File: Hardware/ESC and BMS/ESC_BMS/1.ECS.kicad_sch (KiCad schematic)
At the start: 49 parts, among them Q201 SiR696DP, Q202 SiR696DP, Q203 SiR696DP, Q204 SiR696DP, Q205 SiR696DP, Q206 SiR696DP, U201 74AUC2G08, U202 74AUC2G08, U203 IR2301, U204 IR2301, U205 SN74LVC1G00DBV, U206 SN74LVC1G00DBV, U207 74AUC2G08, U208 TL331, U209 IR2301, U210 SN74LVC1G00DBV

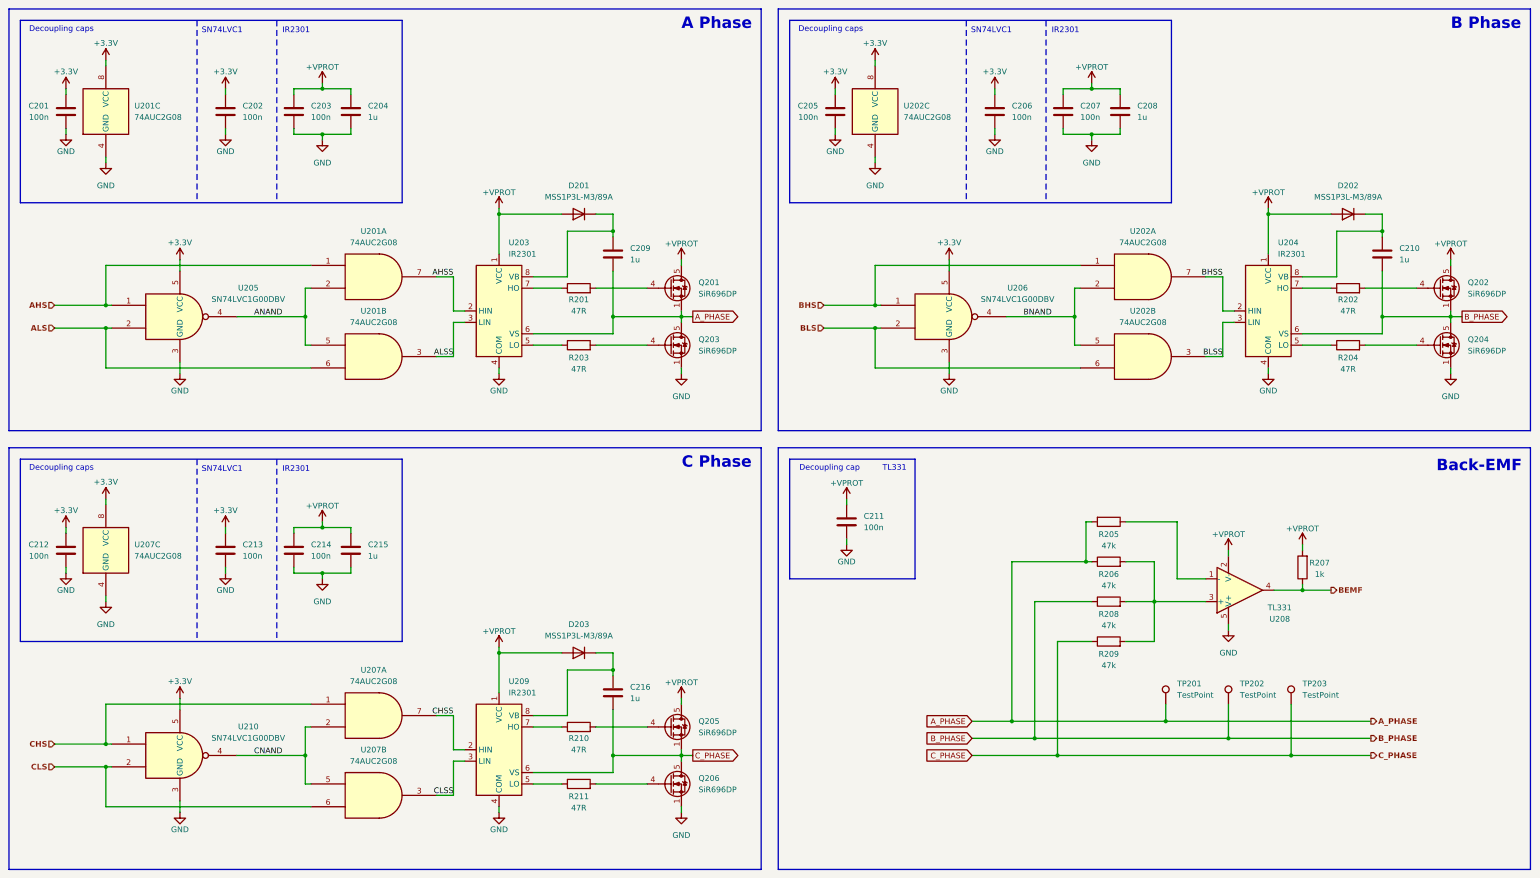
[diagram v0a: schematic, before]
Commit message: Updated 1.ECS.kicad_sch to put more caps and fix some nets
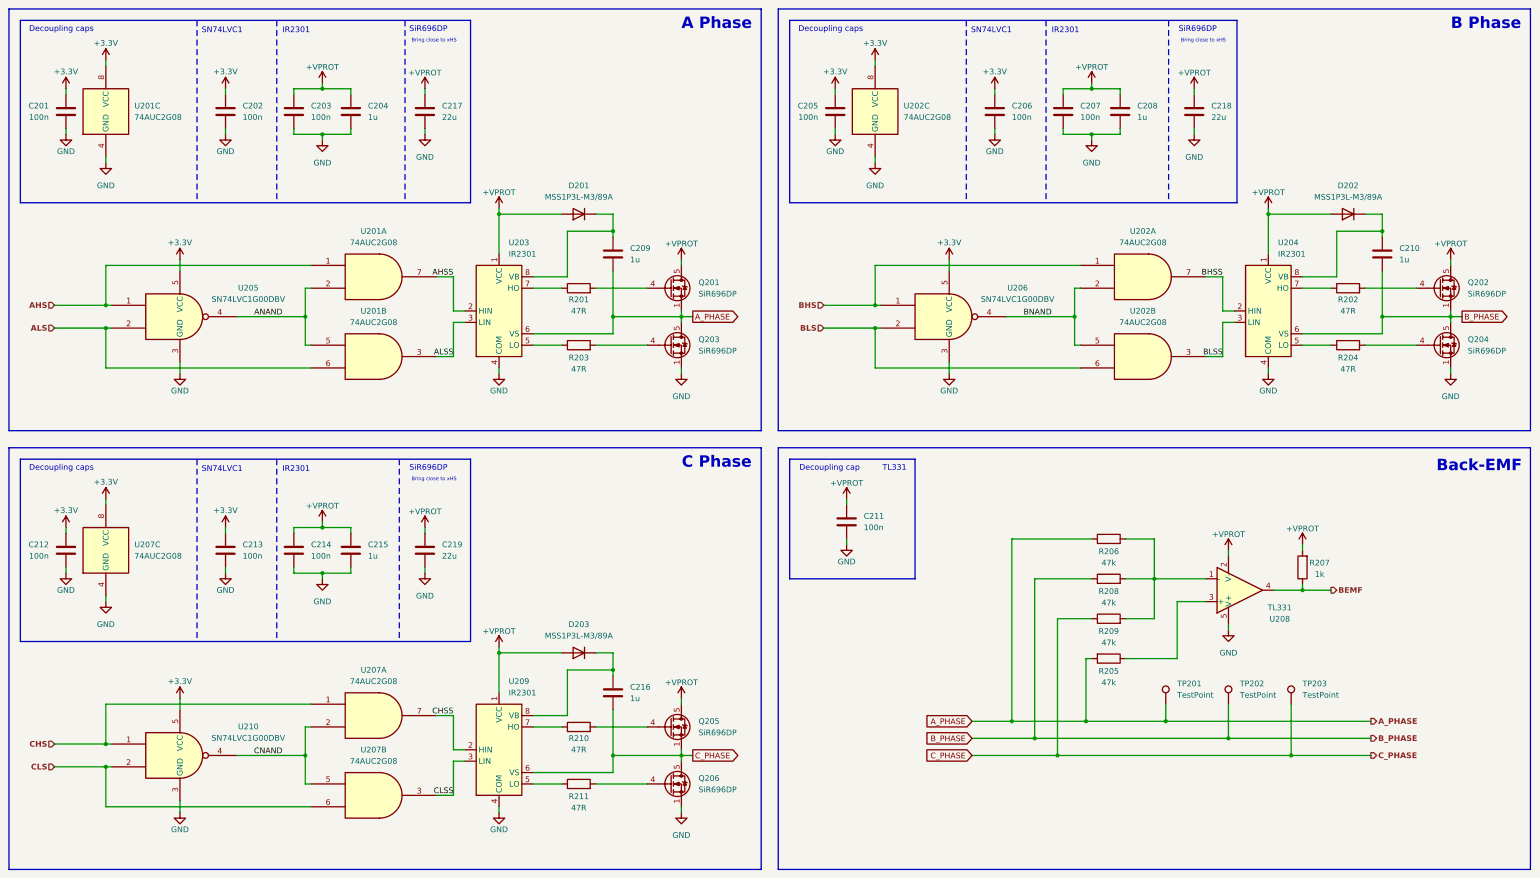
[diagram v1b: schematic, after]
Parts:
- added C217, C218, C219: 22u, Capacitor_SMD:C_0805_2012Metric_Pad1.18x1.45mm_HandSolder, symbol Device:C
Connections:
- net +VPROT: now also C217.1, C218.1, C219.1
- net GND: now also C217.2, C218.2, C219.2
- net at R206.2, R208.2, R209.2: now also U208.1 (-); no longer U208.3 (+)
- net at R205.1: now also U208.3 (+); no longer U208.1 (-)
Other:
- note added: "Bring close to xHS"
- note added: "SiR696DP"
- moved on the sheet: R205, R206, R208, R209

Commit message: initial BMS work
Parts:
- renumbered C217 to C10, C219 to C11, C209 to C12, C216 to C13, C205 to C14, C211 to C15, C206 to C16, C207 to C17, C208 to C18, C218 to C19, C201 to C2, C210 to C20, C212 to C3, C202 to C4, C213 to C5, C203 to C6, C214 to C7, C204 to C8, C215 to C9, D201 to D2, D203 to D3, D202 to D4, Q201 to Q2, Q203 to Q3, Q205 to Q4, Q206 to Q5, Q202 to Q6, Q204 to Q7, R207 to R10, R202 to R11, R204 to R12, R201 to R2, R203 to R3, R210 to R4, R211 to R5, R206 to R6, R208 to R7, R209 to R8, R205 to R9, TP201 to TP2, TP202 to TP3, TP203 to TP4, U208 to U10, U204 to U11, U201 to U2, U207 to U3, U205 to U4, U210 to U5, U203 to U6, U209 to U7, U202 to U8, U206 to U9
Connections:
- net +3.3V: now also R10.2
- net +VPROT: no longer R10.2

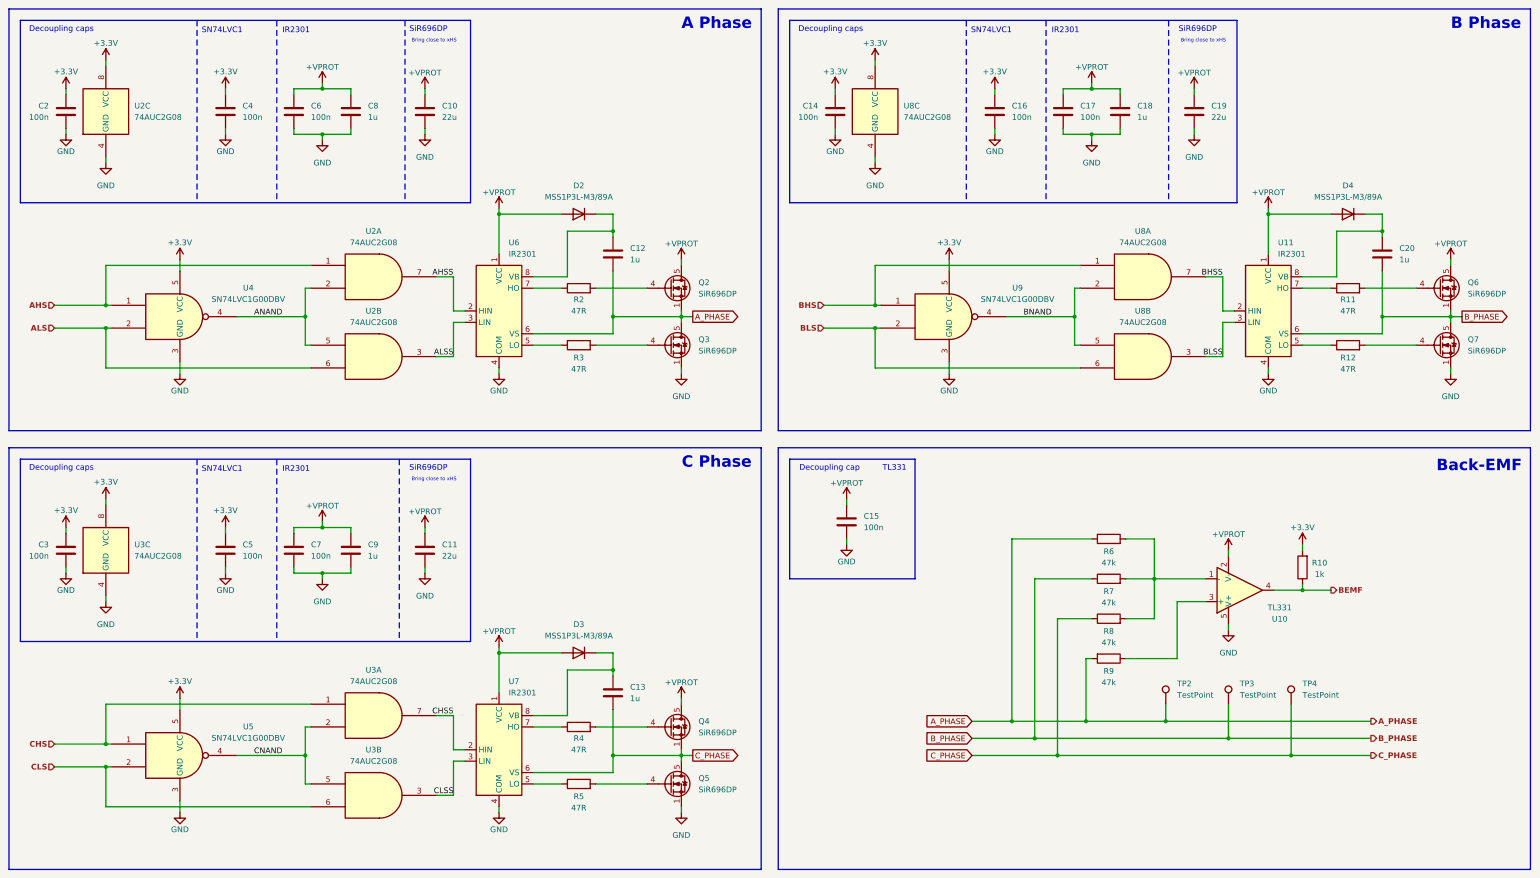
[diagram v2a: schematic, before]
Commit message: Simulations for BMS start and footprints
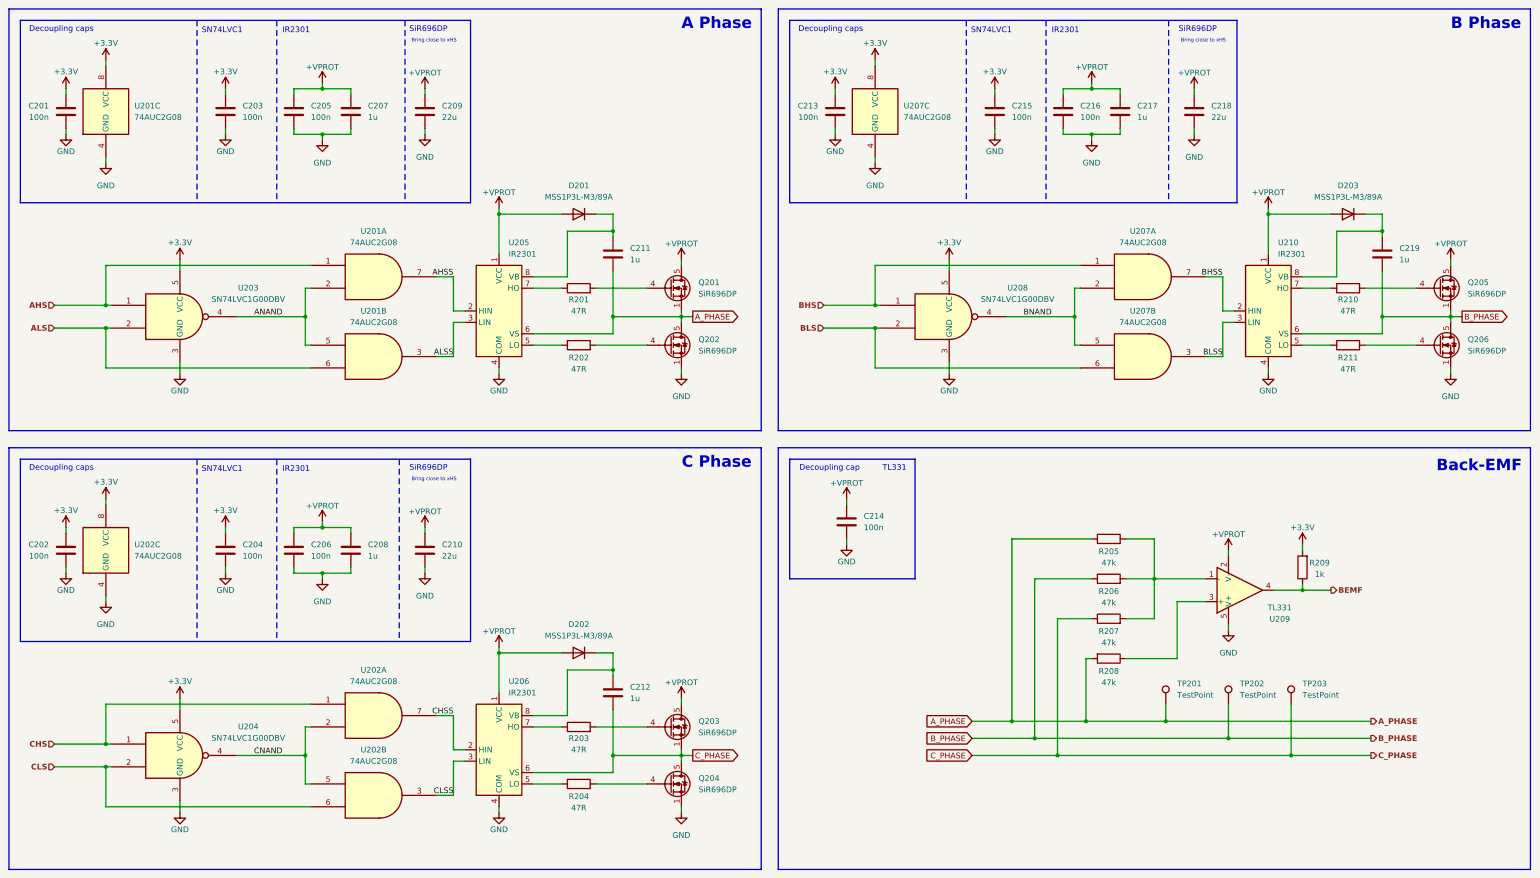
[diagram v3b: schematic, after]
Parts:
- renumbered C2 to C201, C3 to C202, C4 to C203, C5 to C204, C6 to C205, C7 to C206, C8 to C207, C9 to C208, C10 to C209, C11 to C210, C12 to C211, C13 to C212, C14 to C213, C15 to C214, C16 to C215, C17 to C216, C18 to C217, C19 to C218, C20 to C219, D2 to D201, D3 to D202, D4 to D203, Q2 to Q201, Q3 to Q202, Q4 to Q203, Q5 to Q204, Q6 to Q205, Q7 to Q206, R2 to R201, R3 to R202, R4 to R203, R5 to R204, R6 to R205, R7 to R206, R8 to R207, R9 to R208, R10 to R209, R11 to R210, R12 to R211, TP2 to TP201, TP3 to TP202, TP4 to TP203, U2 to U201, U3 to U202, U4 to U203, U5 to U204, U6 to U205, U7 to U206, U8 to U207, U9 to U208, U10 to U209, U11 to U210

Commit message: More BMS
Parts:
- TP201, TP202, TP203: footprint (none) -> TestPoint:TestPoint_Pad_D2.0mm
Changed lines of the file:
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@@
 			)
 		)
-		(property "Footprint" ""
+		(property "Footprint" "TestPoint:TestPoint_Pad_D2.0mm"
 			(at 317.5 196.85 0)
 			(effects
@@
 			)
 		)
-		(property "Footprint" ""
+		(property "Footprint" "TestPoint:TestPoint_Pad_D2.0mm"
 			(at 303.53 196.85 0)
 			(effects
@@
 			)
 		)
-		(property "Footprint" ""
+		(property "Footprint" "TestPoint:TestPoint_Pad_D2.0mm"
 			(at 331.47 196.85 0)
 			(effects

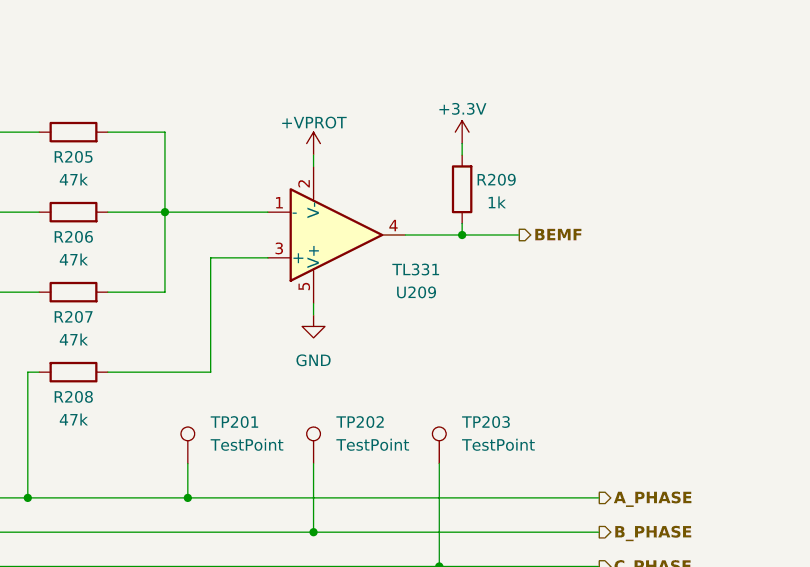
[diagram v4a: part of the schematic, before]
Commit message: ESC/BMS PCB started
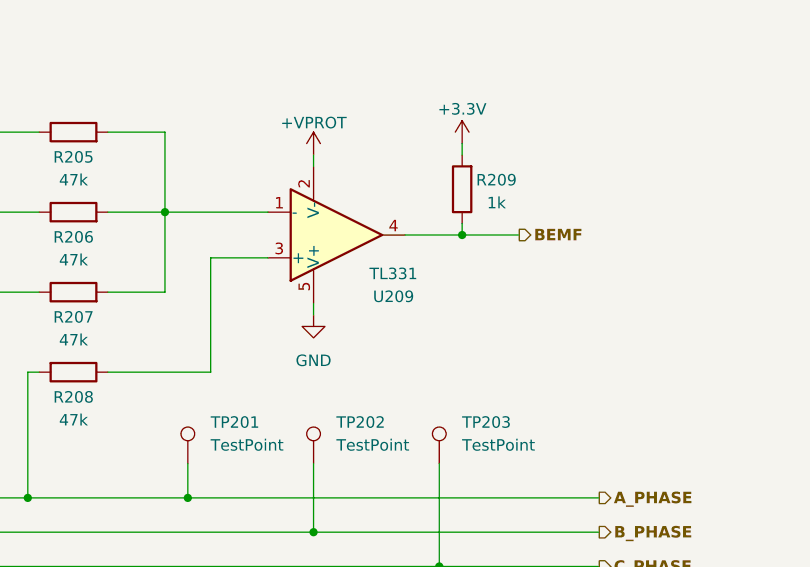
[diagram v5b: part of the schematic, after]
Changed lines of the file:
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@@
 		(dnp no)
 		(property "Reference" "U209"
-			(at 323.85 177.8702 0)
+			(at 321.31 178.308 0)
 			(effects
 				(font
@@
 		)
 		(property "Value" "TL331"
-			(at 323.85 175.3302 0)
+			(at 321.31 175.768 0)
 			(effects
 				(font

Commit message: ESC/BMS board done fully fully
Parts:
- TP201, TP202, TP203: footprint TestPoint:TestPoint_Pad_D2.0mm -> TestPoint:TestPoint_Pad_D1.0mm
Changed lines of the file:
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@@
 			)
 		)
-		(property "Footprint" "TestPoint:TestPoint_Pad_D2.0mm"
+		(property "Footprint" "TestPoint:TestPoint_Pad_D1.0mm"
 			(at 317.5 196.85 0)
 			(effects
@@
 			)
 		)
-		(property "Footprint" "TestPoint:TestPoint_Pad_D2.0mm"
+		(property "Footprint" "TestPoint:TestPoint_Pad_D1.0mm"
 			(at 303.53 196.85 0)
 			(effects
@@
 			)
 		)
-		(property "Footprint" "TestPoint:TestPoint_Pad_D2.0mm"
+		(property "Footprint" "TestPoint:TestPoint_Pad_D1.0mm"
 			(at 331.47 196.85 0)
 			(effects

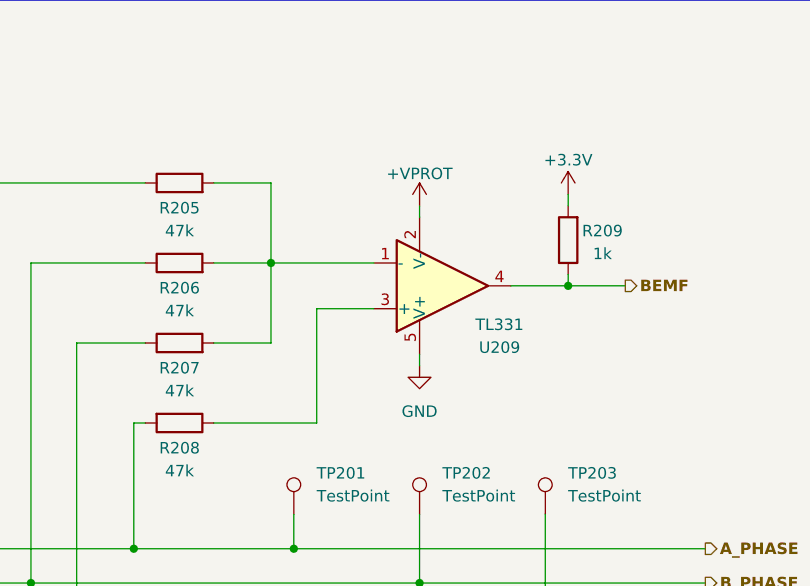
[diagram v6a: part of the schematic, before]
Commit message: fixed vprot and gnd comp error
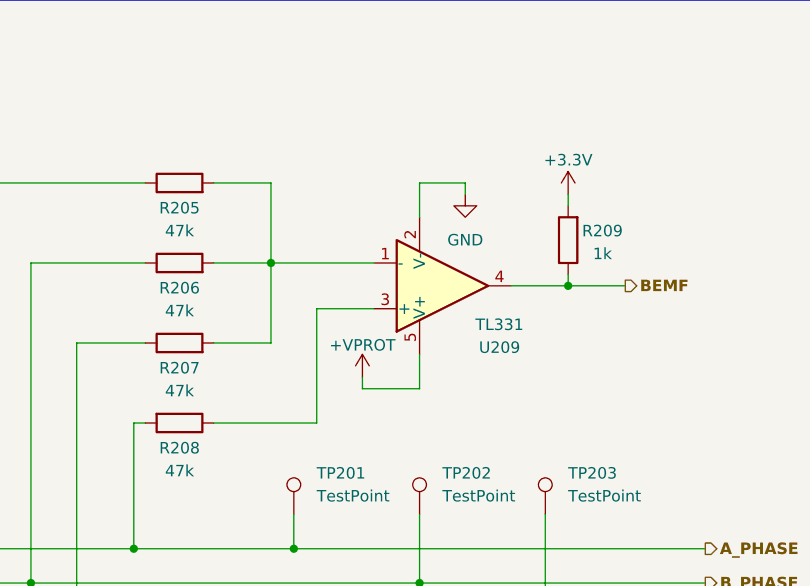
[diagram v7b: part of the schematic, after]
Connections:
- net +VPROT: now also U209.5 (V+); no longer U209.2 (V-)
- net GND: now also U209.2 (V-); no longer U209.5 (V+)
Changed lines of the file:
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@@
 	(wire
 		(pts
+			(xy 312.42 160.02) (xy 312.42 163.83)
+		)
+		(stroke
+			(width 0)
+			(type default)
+		)
+	)
+	(wire
+		(pts
 			(xy 133.35 157.48) (xy 133.35 158.75)
 		)
@@
 	(wire
 		(pts
+			(xy 317.5 160.02) (xy 317.5 161.29)
+		)
+		(stroke
+			(width 0)
+			(type default)
+		)
+	)
+	(wire
+		(pts
 			(xy 104.14 157.48) (xy 104.14 158.75)
 		)
@@
 	(wire
 		(pts
-			(xy 312.42 162.56) (xy 312.42 163.83)
-		)
-		(stroke
-			(width 0)
-			(type default)
-		)
-	)
-	(wire
-		(pts
 			(xy 224.79 68.58) (xy 224.79 69.85)
 		)
@@
 	(wire
 		(pts
+			(xy 312.42 179.07) (xy 312.42 182.88)
+		)
+		(stroke
+			(width 0)
+			(type default)
+		)
+	)
+	(wire
+		(pts
 			(xy 135.89 217.17) (xy 139.7 217.17)
 		)
@@
 	(wire
 		(pts
+			(xy 306.07 182.88) (xy 312.42 182.88)
+		)
+		(stroke
+			(width 0)
+			(type default)
+		)
+	)
+	(wire
+		(pts
 			(xy 62.23 53.34) (xy 62.23 54.61)
 		)
@@
 	(wire
 		(pts
+			(xy 306.07 181.61) (xy 306.07 182.88)
+		)
+		(stroke
+			(width 0)
+			(type default)
+		)
+	)
+	(wire
+		(pts
 			(xy 289.56 177.8) (xy 295.91 177.8)
 		)
@@
 	(wire
 		(pts
+			(xy 312.42 160.02) (xy 317.5 160.02)
+		)
+		(stroke
+			(width 0)
+			(type default)
+		)
+	)
+	(wire
+		(pts
 			(xy 222.25 107.95) (xy 233.68 107.95)
 		)
@@
 	(wire
 		(pts
-			(xy 312.42 179.07) (xy 312.42 180.34)
-		)
-		(stroke
-			(width 0)
-			(type default)
-		)
-	)
-	(wire
-		(pts
 			(xy 78.74 218.44) (xy 78.74 220.98)
 		)
@@
 	(symbol
 		(lib_id "power:GND")
-		(at 312.42 180.34 0)
+		(at 317.5 161.29 0)
 		(unit 1)
 		(exclude_from_sim no)
@@
 		(fields_autoplaced yes)
 		(property "Reference" "#PWR0248"
-			(at 312.42 186.69 0)
+			(at 317.5 167.64 0)
 			(effects
 				(font
@@
 		)
 		(property "Value" "GND"
-			(at 312.42 185.42 0)
+			(at 317.5 166.37 0)
 			(effects
 				(font
@@
 		)
 		(property "Footprint" ""
-			(at 312.42 180.34 0)
+			(at 317.5 161.29 0)
 			(effects
 				(font
@@
 		)
 		(property "Datasheet" ""
-			(at 312.42 180.34 0)
+			(at 317.5 161.29 0)
 			(effects
 				(font
@@
 		)
 		(property "Description" "Power symbol creates a global label with name \"GND\" , ground"
-			(at 312.42 180.34 0)
+			(at 317.5 161.29 0)
 			(effects
 				(font
@@
 		)
 		(instances
-			(project ""
+			(project "SPROJ3EE_ESC_BMS"
 				(path "/64aee9f2-a448-43ef-b28d-f00e276bd9f5/cbf19aec-b6c8-49c6-ab18-d6d5f10759f9"
 					(reference "#PWR0248")
@@
 	(symbol
 		(lib_id "power:VBUS")
-		(at 312.42 162.56 0)
+		(at 306.07 181.61 0)
 		(unit 1)
 		(exclude_from_sim no)
@@
 		(dnp no)
 		(property "Reference" "#PWR0247"
-			(at 312.42 166.37 0)
+			(at 306.07 185.42 0)
 			(effects
 				(font
@@
 		)
 		(property "Value" "+VPROT"
-			(at 312.42 159.004 0)
+			(at 306.07 178.054 0)
 			(effects
 				(font
@@
 		)
 		(property "Footprint" ""
-			(at 312.42 162.56 0)
+			(at 306.07 181.61 0)
 			(effects
 				(font
@@
 		)
 		(property "Datasheet" ""
-			(at 312.42 162.56 0)
+			(at 306.07 181.61 0)
 			(effects
 				(font
@@
 		)
 		(property "Description" "Power symbol creates a global label with name \"VBUS\""
-			(at 312.42 162.56 0)
+			(at 306.07 181.61 0)
 			(effects
 				(font
